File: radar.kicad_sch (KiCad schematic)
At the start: 7 parts, among them J1 USB_C_Receptacle, J2 JST, U1 BQ25895RTW

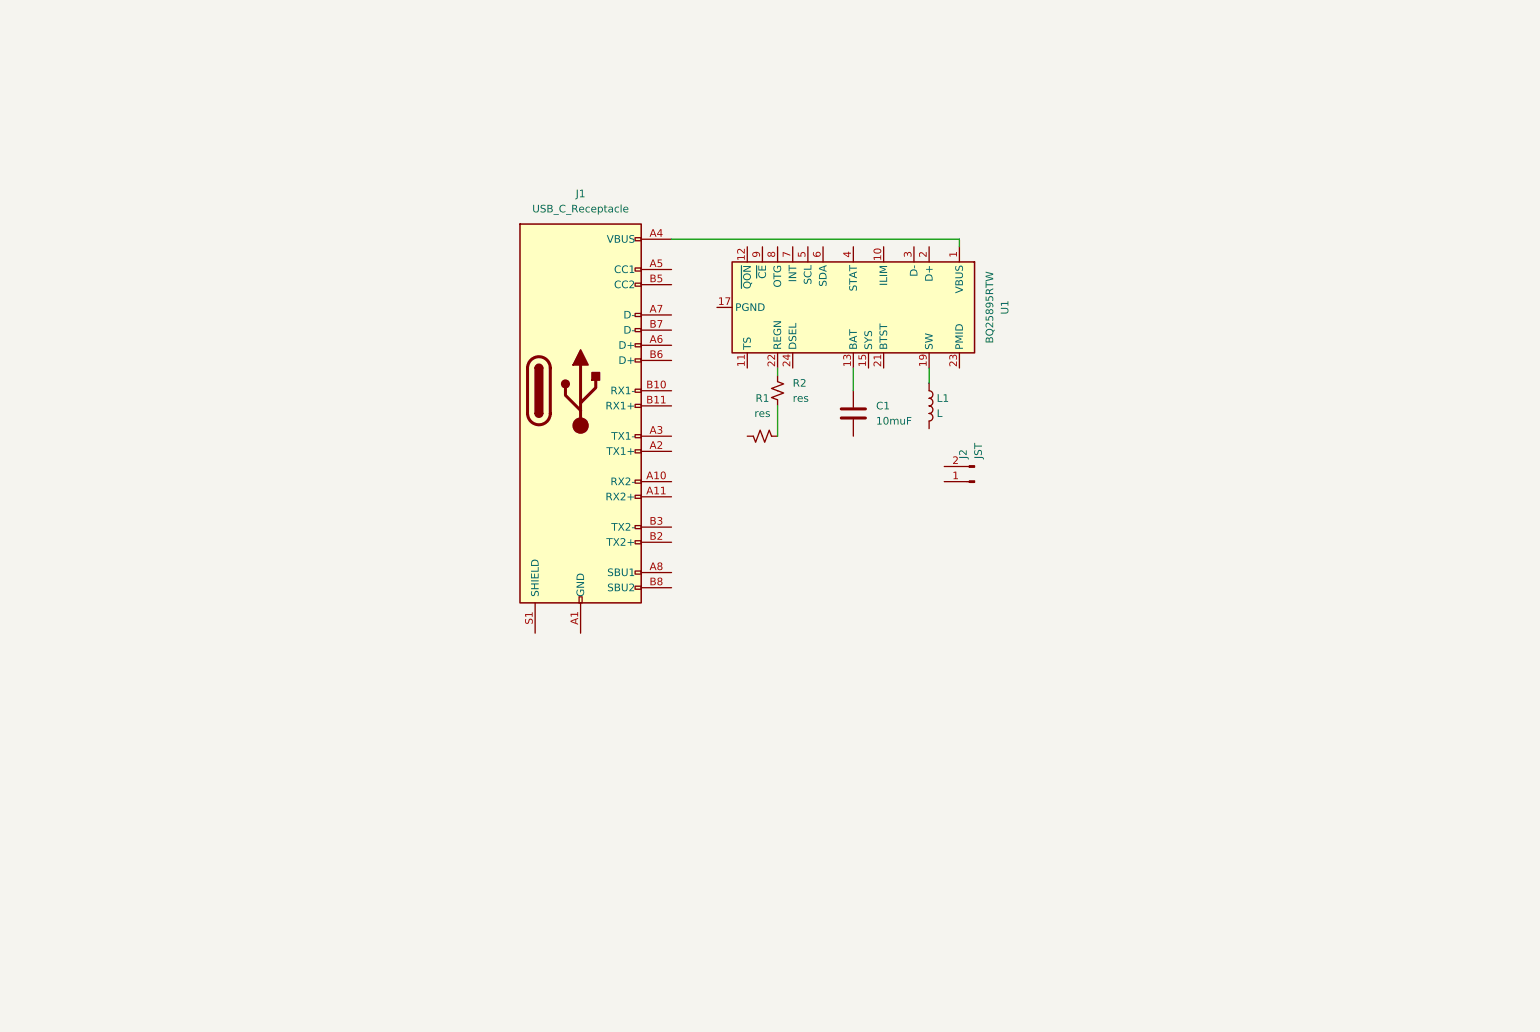
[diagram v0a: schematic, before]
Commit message: finished power sheet
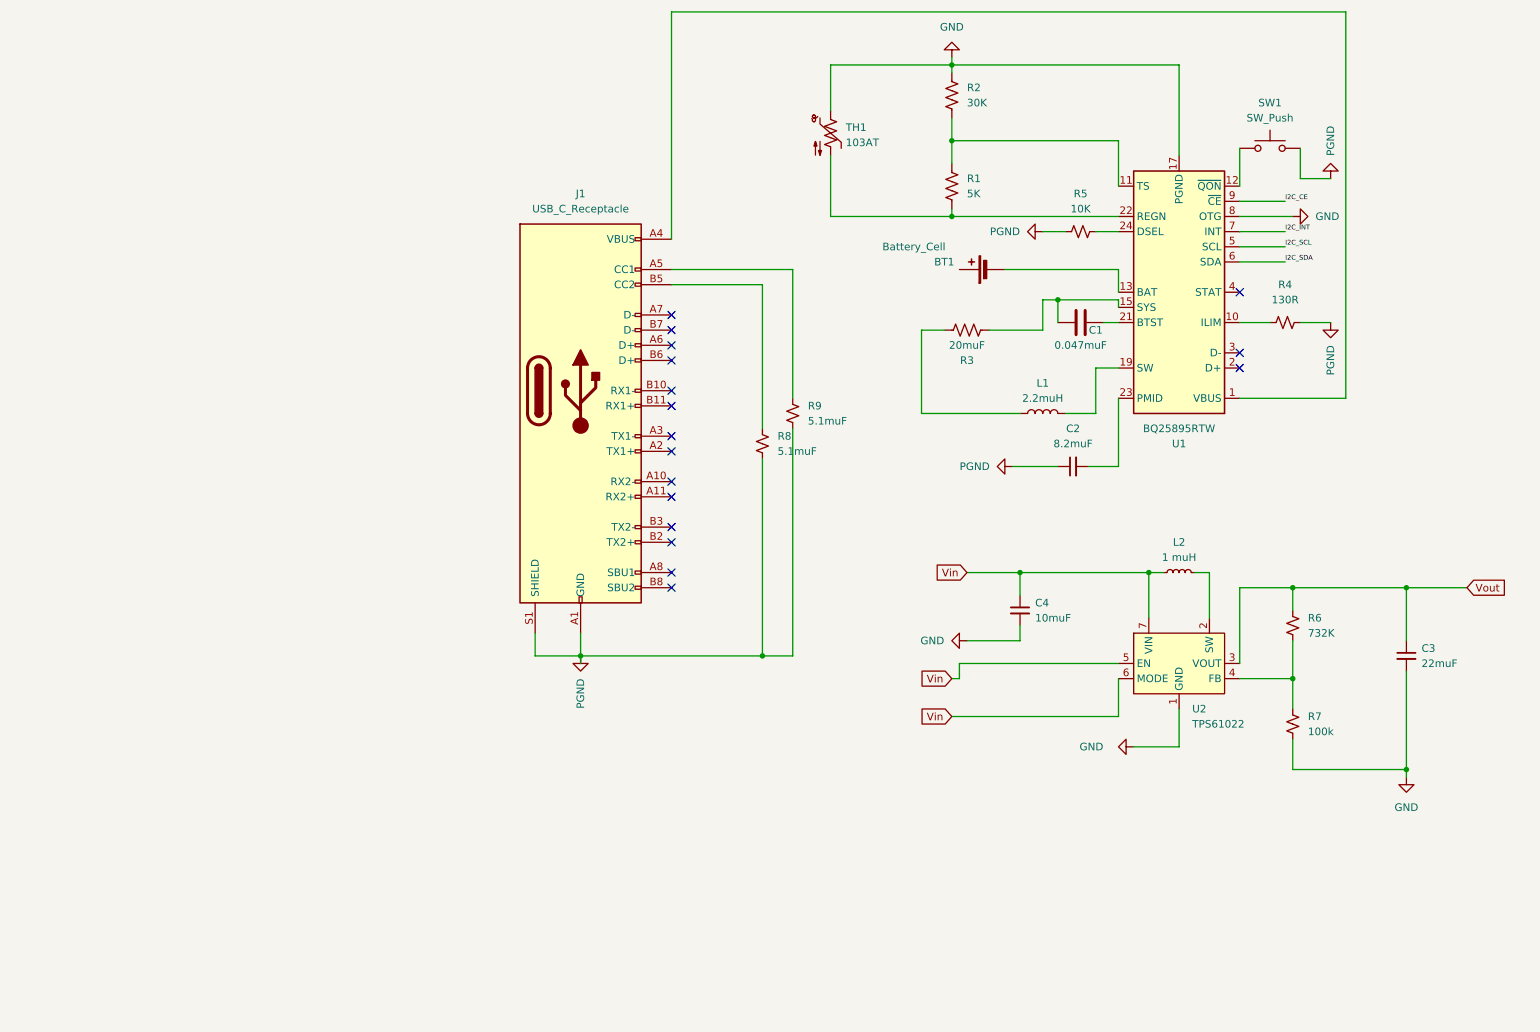
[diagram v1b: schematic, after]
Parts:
- removed J2: JST, symbol Connector:Conn_01x02_Pin
- removed R1, R2: res, symbol Device:R_Small_US
- added BT1: Battery_Cell, symbol Device:Battery_Cell
- added C2: 8.2muF, symbol Device:C_Small
- added C3: 22muF, symbol Device:C_Small
- added C4: 10muF, symbol Device:C_Small
- added L2: 1 muH, symbol Device:L_Small
- added R1: 5K, symbol Device:R_US
- added R2: 30K, symbol Device:R_US
- added R3: 20muF, symbol Device:R_US
- added R4: 130R, symbol Device:R_Small_US
- added R5: 10K, symbol Device:R_Small_US
- added R6: 732K, symbol Device:R_Small_US
- added R7: 100k, symbol Device:R_Small_US
- added R8, R9: 5.1muF, symbol Device:R_Small_US
- added SW1: SW_Push, symbol Switch:SW_Push
- added TH1: 103AT, symbol Device:Thermistor_NTC_US
- added U2: TPS61022, Package_DFN_QFN:Texas_RWU0007A_VQFN-7_2x2mm_P0.5mm, symbol Converter_DCDC:TPS61022
- C1: value 10muF -> 0.047muF
- L1: value L -> 2.2muH
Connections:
- net at U1.19 (SW), U1.20 (SW): now also L1.2; no longer L1.1
- net at U1.22 (REGN): now also R1.2, TH1.2
- net GND: now reaches J1.A1 (GND), J1.A12 (GND), J1.B1 (GND), J1.B12 (GND)
- net GND: now also J1.S1 (SHIELD), U1.17 (PGND), U1.18 (PGND), U1.25 (PGND), U1.8 (OTG), C2.1, C3.2, C4.2, R2.1, R4.2, R5.1, R7.2, R8.1, R9.2, SW1.2, TH1.1, U2.1 (GND)
- net at J1.A5 (CC1): now also R9.1
- net at J1.B5 (CC2): now also R8.2
- net at U1.13 (BAT), U1.14 (BAT): now also BT1.2 (-); no longer C1.1
- net at C1.2: now also U1.21 (BTST)
- net at U1.10 (ILIM): now also R4.1
- net at U1.11 (TS): now also R1.1, R2.2
- net at U1.12 (~{QON}): now also SW1.1
- net at U1.15 (SYS), U1.16 (SYS): now also C1.1, R3.2
- net at U1.23 (PMID): now also C2.2
- net at U1.24 (DSEL): now also R5.2
- net I2C_SCL: now reaches U1.5 (SCL)
- net I2C_SDA: now reaches U1.6 (SDA)
- net I2C_INT: now reaches U1.7 (INT)
- net I2C_CE: now reaches U1.9 (~{CE})
- new net: L2.2, U2.2 (SW)
- new net: R6.2, R7.1, U2.4 (FB)
- new net: L1.1, R3.1
- new net Vin: C4.1, L2.1, U2.5 (EN), U2.6 (MODE), U2.7 (VIN)
- new net Vout: C3.1, R6.1, U2.3 (VOUT)
- no-connect marks 0 -> 17
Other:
- moved on the sheet: U1

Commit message: working on power again with new compoenets
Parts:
- removed BT1: Battery_Cell, symbol Device:Battery_Cell
- removed C1: 0.047muF, symbol Device:C
- removed C2: 8.2muF, symbol Device:C_Small
- removed C3: 22muF, symbol Device:C_Small
- removed C4: 10muF, symbol Device:C_Small
- removed J1: USB_C_Receptacle, symbol Connector:USB_C_Receptacle
- removed L1: 2.2muH, symbol Device:L
- removed L2: 1 muH, symbol Device:L_Small
- removed R1: 5K, symbol Device:R_US
- removed R2: 30K, symbol Device:R_US
- removed R3: 20muF, symbol Device:R_US
- removed R4: 130R, symbol Device:R_Small_US
- removed R5: 10K, symbol Device:R_Small_US
- removed R6: 732K, symbol Device:R_Small_US
- removed R7: 100k, symbol Device:R_Small_US
- removed R8, R9: 5.1muF, symbol Device:R_Small_US
- removed SW1: SW_Push, symbol Switch:SW_Push
- removed TH1: 103AT, symbol Device:Thermistor_NTC_US
- removed U1: BQ25895RTW, Package_DFN_QFN:Texas_RTW_WQFN-24-1EP_4x4mm_P0.5mm_EP2.7x2.7mm_ThermalVias, symbol Battery_Management:BQ25895RTW
- removed U2: TPS61022, Package_DFN_QFN:Texas_RWU0007A_VQFN-7_2x2mm_P0.5mm, symbol Converter_DCDC:TPS61022
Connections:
- no-connect marks 17 -> 0
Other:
- added sheet awr1843 (awr1843.kicad_sch)
- added sheet power (Power.kicad_sch)
- added sheet stm32h7_core (stm32h7_core.kicad_sch)

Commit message: working on connectors
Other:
- removed sheet stm32h7_core
- note added: "All PMICs of the board"
- note added: "The brain, functions as the MCU & RF signal TX/RX"
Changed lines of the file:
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@@
 (kicad_sch (version 20230121) (generator eeschema)
   (paper "A4")
-  (sheet (at 92.71 30.48) (size 50.8 22.86) (fields_autoplaced)
+  (text "The brain, functions as the MCU & RF signal TX/RX" (at 97.79 26.67 0)
+    (effects (font (size 2 2)) (justify left bottom))
+  )
+  (text "All PMICs of the board" (at 31.75 62.23 0)
+    (effects (font (size 2 2)) (justify left bottom))
+  )
+  (sheet (at 17.78 66.04) (size 62.23 39.37) (fields_autoplaced)
     (stroke (width 0.1524) (type solid))
     (fill (color 0 0 0 0.0000))
-    (property "Sheetname" "stm32h7_core" (at 92.71 29.7684 0)
+    (property "Sheetname" "power" (at 17.78 65.3284 0)
       (effects (font (size 1.27 1.27)) (justify left bottom))
     )
-    (property "Sheetfile" "stm32h7_core.kicad_sch" (at 92.71 53.9246 0)
+    (property "Sheetfile" "Power.kicad_sch" (at 17.78 105.9946 0)
       (effects (font (size 1.27 1.27)) (justify left top))
     )
-    (instances
-      (project "radar"
-        (path "/88b309aa-5f0e-45d7-beec-81d4b0ee2121" (page "3"))
-      )
-    )
-  )
-  (sheet (at 34.29 29.21) (size 45.72 24.13) (fields_autoplaced)
-    (stroke (width 0.1524) (type solid))
-    (fill (color 0 0 0 0.0000))
-    (property "Sheetname" "power" (at 34.29 28.4984 0)
-      (effects (font (size 1.27 1.27)) (justify left bottom))
-    )
-    (property "Sheetfile" "Power.kicad_sch" (at 34.29 53.9246 0)
-      (effects (font (size 1.27 1.27)) (justify left top))
-    )
-    (property "Field2" "" (at 34.29 29.21 0)
+    (property "Field2" "" (at 17.78 66.04 0)
       (effects (font (size 1.27 1.27)) hide)
     )
@@
     )
   )
-  (sheet (at 43.18 81.28) (size 87.63 39.37) (fields_autoplaced)
+  (sheet (at 92.71 30.48) (size 87.63 39.37) (fields_autoplaced)
     (stroke (width 0.1524) (type solid))
     (fill (color 0 0 0 0.0000))
-    (property "Sheetname" "awr1843" (at 43.18 80.5684 0)
+    (property "Sheetname" "awr1843" (at 92.71 29.7684 0)
       (effects (font (size 1.27 1.27)) (justify left bottom))
     )
-    (property "Sheetfile" "awr1843.kicad_sch" (at 43.18 121.2346 0)
+    (property "Sheetfile" "awr1843.kicad_sch" (at 92.71 70.4346 0)
       (effects (font (size 1.27 1.27)) (justify left top))
     )

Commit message: grabbing flash footprint and symbol
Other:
- added sheet connectors (cntors.kicad_sch)
- added sheet flash (16flashmem.kicad_sch)
- note added: "Connectors"
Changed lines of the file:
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@@
 (kicad_sch (version 20230121) (generator eeschema)
   (paper "A4")
-  (text "The brain, functions as the MCU & RF signal TX/RX" (at 97.79 26.67 0)
+  (text "The brain, functions as the MCU & RF signal TX/RX" (at 21.59 78.74 0)
     (effects (font (size 2 2)) (justify left bottom))
   )
-  (text "All PMICs of the board" (at 31.75 62.23 0)
+  (text "All PMICs of the board" (at 36.83 140.97 0)
     (effects (font (size 2 2)) (justify left bottom))
   )
-  (sheet (at 17.78 66.04) (size 62.23 39.37) (fields_autoplaced)
+  (text "Connectors\n" (at 204.47 107.95 0)
+    (effects (font (size 2 2)) (justify left bottom))
+  )
+  (sheet (at 24.13 143.51) (size 62.23 39.37) (fields_autoplaced)
     (stroke (width 0.1524) (type solid))
     (fill (color 0 0 0 0.0000))
-    (property "Sheetname" "power" (at 17.78 65.3284 0)
+    (property "Sheetname" "power" (at 24.13 142.7984 0)
       (effects (font (size 1.27 1.27)) (justify left bottom))
     )
-    (property "Sheetfile" "Power.kicad_sch" (at 17.78 105.9946 0)
+    (property "Sheetfile" "Power.kicad_sch" (at 24.13 183.4646 0)
       (effects (font (size 1.27 1.27)) (justify left top))
     )
-    (property "Field2" "" (at 17.78 66.04 0)
+    (property "Field2" "" (at 24.13 143.51 0)
       (effects (font (size 1.27 1.27)) hide)
     )
@@
     )
   )
-  (sheet (at 92.71 30.48) (size 87.63 39.37) (fields_autoplaced)
+  (sheet (at 153.67 34.29) (size 88.9 41.91) (fields_autoplaced)
     (stroke (width 0.1524) (type solid))
     (fill (color 0 0 0 0.0000))
-    (property "Sheetname" "awr1843" (at 92.71 29.7684 0)
+    (property "Sheetname" "flash" (at 153.67 33.5784 0)
       (effects (font (size 1.27 1.27)) (justify left bottom))
     )
-    (property "Sheetfile" "awr1843.kicad_sch" (at 92.71 70.4346 0)
+    (property "Sheetfile" "16flashmem.kicad_sch" (at 153.67 76.7846 0)
+      (effects (font (size 1.27 1.27)) (justify left top))
+    )
+    (instances
+      (project "radar"
+        (path "/88b309aa-5f0e-45d7-beec-81d4b0ee2121" (page "6"))
+      )
+    )
+  )
+  (sheet (at 16.51 82.55) (size 87.63 39.37) (fields_autoplaced)
+    (stroke (width 0.1524) (type solid))
+    (fill (color 0 0 0 0.0000))
+    (property "Sheetname" "awr1843" (at 16.51 81.8384 0)
+      (effects (font (size 1.27 1.27)) (justify left bottom))
+    )
+    (property "Sheetfile" "awr1843.kicad_sch" (at 16.51 122.5046 0)
       (effects (font (size 1.27 1.27)) (justify left top))
     )
@@
       )
     )
+  )
+  (sheet (at 160.02 111.76) (size 110.49 45.72) (fields_autoplaced)
+    (stroke (width 0.1524) (type solid))
+    (fill (color 0 0 0 0.0000))
+    (property "Sheetname" "connectors" (at 160.02 111.0484 0)
+      (effects (font (size 1.27 1.27)) (justify left bottom))
+    )
+    (property "Sheetfile" "cntors.kicad_sch" (at 160.02 158.0646 0)
+      (effects (font (size 1.27 1.27)) (justify left top))
+    )
+    (instances
+      (project "radar"
+        (path "/88b309aa-5f0e-45d7-beec-81d4b0ee2121" (page "5"))
+      )
+    )
